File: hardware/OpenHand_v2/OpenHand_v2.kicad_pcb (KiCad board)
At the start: 4 copper layers, 100 x 50 mm, 177 parts, among them J1 CONN_MOTOR_1, J10 CONN_FDBK_2, J2 CONN_MOTOR_2, J3 CONN_BATT, J5 USB_C_CONN, J6 CONN_MOTOR_3, J7 CONN_FDBK_1, Q1 AO3401A, SW1 BTN_RST, SW3 SW_Push, U1 STM32F103RETx, U10 DRV8833PWP, U2 TPS565201DDCR, U3 AMS1117-3.3, U4 LT1175-5_SOT223, U5 LM324, U6 LM324, U7 DRV8833PWP, U8 DRV8833PWP, U9 DRV8833PWP

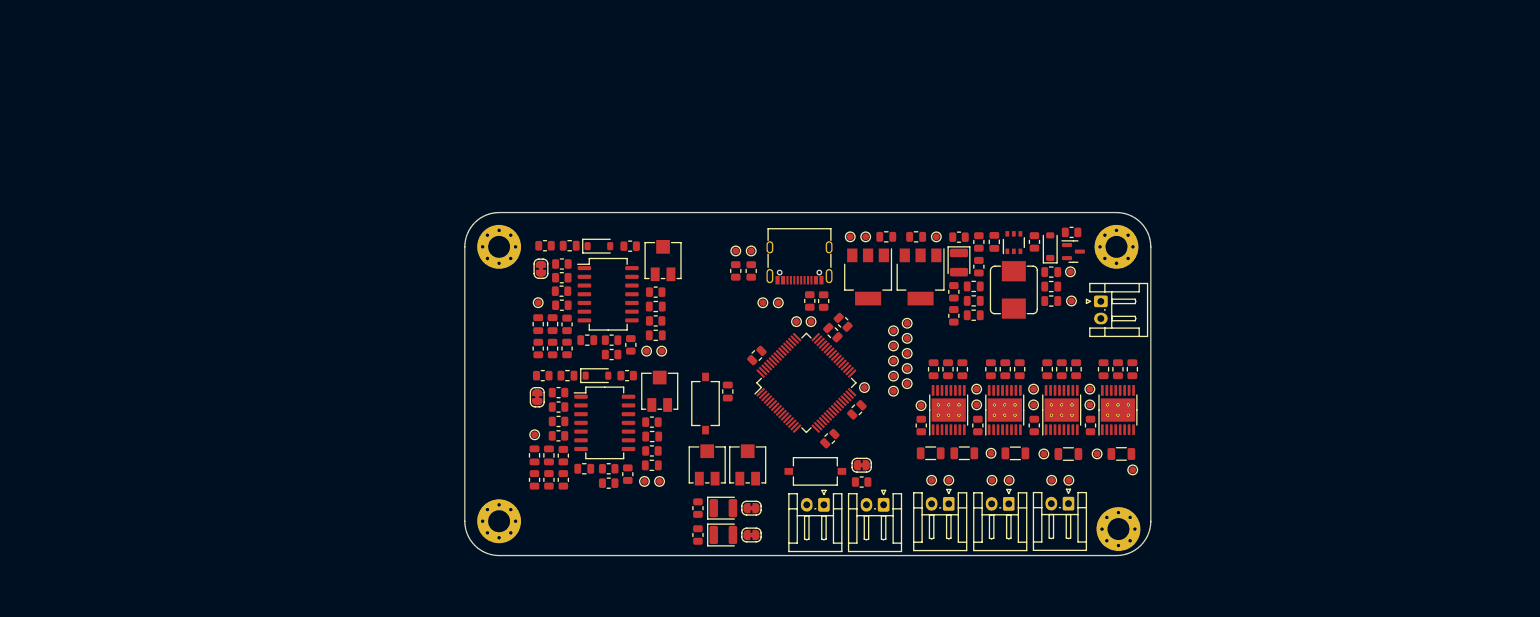
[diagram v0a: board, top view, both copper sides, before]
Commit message: Update V2 schematic and start PCB layout
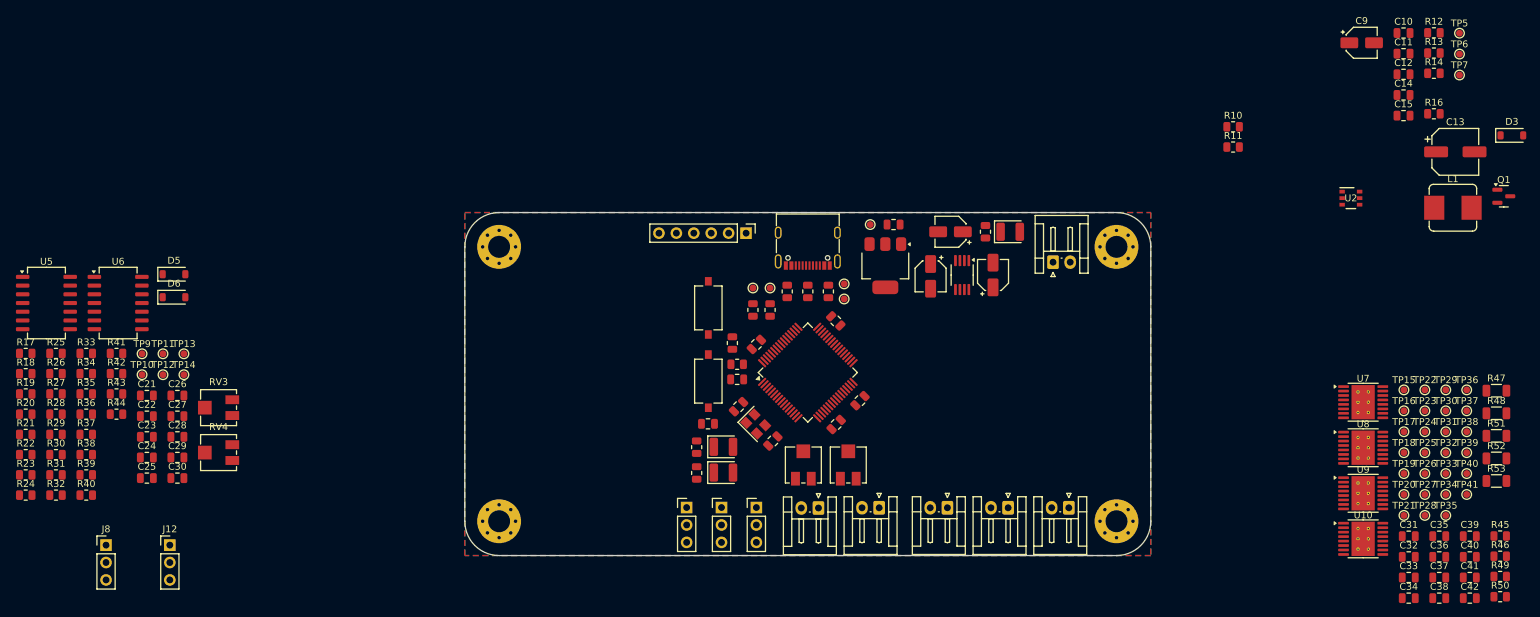
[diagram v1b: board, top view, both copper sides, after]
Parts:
- removed C18: 470n, Capacitor_SMD:C_0805_2012Metric
- removed JP15: JMPR_EMG_1_UC, Jumper:SolderJumper-2_P1.3mm_Bridged_RoundedPad1.0x1.5mm
- removed JP16: JMPR_EMG_2_UC, Jumper:SolderJumper-2_P1.3mm_Bridged_RoundedPad1.0x1.5mm
- removed JP2: JMPR_LED_1, Jumper:SolderJumper-2_P1.3mm_Bridged_RoundedPad1.0x1.5mm
- removed JP3: JMPR_BTN_1, Jumper:SolderJumper-2_P1.3mm_Bridged_RoundedPad1.0x1.5mm
- removed JP4: JMPR_LED_2, Jumper:SolderJumper-2_P1.3mm_Bridged_RoundedPad1.0x1.5mm
- removed R54, R55, R59: 0R2, Resistor_SMD:R_1206_3216Metric
- removed R56, R57: 10k, Resistor_SMD:R_0805_2012Metric
- removed R58, R60: 4R7, Resistor_SMD:R_1206_3216Metric
- removed RV5: 100k, Potentiometer_SMD:Potentiometer_Vishay_TS53YJ_Vertical
- removed SW3: SW_Push, Button_Switch_SMD:SW_Tactile_SPST_NO_Straight_CK_PTS636Sx25SMTRLFS
- removed TP42: TP_MOT_2_UC1, TestPoint:TestPoint_Pad_D1.0mm
- removed TP43: TP_MOT_1_UC2, TestPoint:TestPoint_Pad_D1.0mm
- removed TP44: TP_MOT_2_UC2, TestPoint:TestPoint_Pad_D1.0mm
- removed TP45: TP_MOT_1_OUT_P, TestPoint:TestPoint_Pad_D1.0mm
- removed TP46: TP_MOT_2_OUT_P, TestPoint:TestPoint_Pad_D1.0mm
- removed TP47: TP_MOT_1_OUT_N, TestPoint:TestPoint_Pad_D1.0mm
- removed TP48: TP_MOT_2_OUT_N, TestPoint:TestPoint_Pad_D1.0mm
- removed TP49: TP_MOT_3_EN, TestPoint:TestPoint_Pad_D1.0mm
- removed TP50: TP_FDBK_MOT_EN, TestPoint:TestPoint_Pad_D1.0mm
- removed TP51: TP_MOT_3_IS, TestPoint:TestPoint_Pad_D1.0mm
- removed TP52: TP_MOT_3_FAULT, TestPoint:TestPoint_Pad_D1.0mm
- removed TP53: TP_FDBK_MOT_FAULT, TestPoint:TestPoint_Pad_D1.0mm
- removed TP54: TP_MOT_3_UC1, TestPoint:TestPoint_Pad_D1.0mm
- removed TP55: TP_FDBK_MOT_1_UC1, TestPoint:TestPoint_Pad_D1.0mm
- removed TP56: TP_MOT_3_UC2, TestPoint:TestPoint_Pad_D1.0mm
- removed TP57: TP_FDBK_MOT_1_UC2, TestPoint:TestPoint_Pad_D1.0mm
- removed TP58: TP_MOT_3_OUT_P, TestPoint:TestPoint_Pad_D1.0mm
- removed TP59: TP_MOT_3_OUT_N, TestPoint:TestPoint_Pad_D1.0mm
- removed TP60: TP_FDBK_MOT_2_UC1, TestPoint:TestPoint_Pad_D1.0mm
- removed TP61: TP_FDBK_MOT_2_UC2, TestPoint:TestPoint_Pad_D1.0mm
- added C2: 100n, Capacitor_SMD:C_0805_2012Metric, F.Cu at (142.5, 119.2)
- added C40: 10n, Capacitor_SMD:C_0805_2012Metric, F.Cu at (246.5, 150.2)
- added C41: 10u, Capacitor_SMD:C_0805_2012Metric, F.Cu at (246.5, 153.2)
- added C42: 10u, Capacitor_SMD:C_0805_2012Metric, F.Cu at (246.5, 156.2)
- added J11: CONN_FDBK_2, Connector_JST:JST_EH_S2B-EH_1x02_P2.50mm_Horizontal, F.Cu at (160.4, 143.0)
- added J12: CONN_EMG_2, Connector_PinHeader_2.54mm:PinHeader_1x03_P2.54mm_Vertical, F.Cu at (57.0, 148.5)
- added J13: CONN_POS_3, Connector_PinHeader_2.54mm:PinHeader_1x03_P2.54mm_Vertical, F.Cu at (142.5, 143.0)
- added J4: CONN_POS_1, Connector_PinHeader_2.54mm:PinHeader_1x03_P2.54mm_Vertical, F.Cu at (132.3, 143.0)
- added J8: CONN_EMG_1, Connector_PinHeader_2.54mm:PinHeader_1x03_P2.54mm_Vertical, F.Cu at (47.7, 148.5)
- added J9: CONN_POS_2, Connector_PinHeader_2.54mm:PinHeader_1x03_P2.54mm_Vertical, F.Cu at (137.4, 143.0)
- added R1: 5k1, Resistor_SMD:R_0805_2012Metric, F.Cu at (153.0, 111.5)
- added R13: 54.9k, Resistor_SMD:R_0805_2012Metric, F.Cu at (241.3, 76.8)
- added R14: 47k, Resistor_SMD:R_0805_2012Metric, F.Cu at (241.3, 79.7)
- added R15: 4k7, Resistor_SMD:R_0805_2012Metric, F.Cu at (175.9, 102.8)
- added R16: 10k, Resistor_SMD:R_0805_2012Metric, F.Cu at (241.3, 85.6)
- added R5: 4k7, Resistor_SMD:R_0805_2012Metric, F.Cu at (144.5, 114.2)
- added RV3: 100k, Potentiometer_SMD:Potentiometer_Vishay_TS53YJ_Vertical, F.Cu at (64.1, 128.4)
- added SW2: SW_Push, Button_Switch_SMD:SW_Tactile_SPST_NO_Straight_CK_PTS636Sx25SMTRLFS, F.Cu at (135.5, 113.9)
- added TP1: TP_UC_TX, TestPoint:TestPoint_Pad_D1.0mm, F.Cu at (155.3, 110.4)
- added TP10: TP_EMG_2_AMP, TestPoint:TestPoint_Pad_D1.0mm, F.Cu at (53.0, 123.6)
- added TP11: TP_EMG_1_HP, TestPoint:TestPoint_Pad_D1.0mm, F.Cu at (56.0, 120.6)
- added TP12: TP_EMG_2_HP, TestPoint:TestPoint_Pad_D1.0mm, F.Cu at (56.0, 123.6)
- added TP13: TP_EMG_1_LP, TestPoint:TestPoint_Pad_D1.0mm, F.Cu at (59.1, 120.6)
- added TP14: TP_EMG_2_LP, TestPoint:TestPoint_Pad_D1.0mm, F.Cu at (59.1, 123.6)
- added TP15: TP_MOT_1_EN, TestPoint:TestPoint_Pad_D1.0mm, F.Cu at (236.9, 125.8)
- added TP16: TP_MOT_2_EN, TestPoint:TestPoint_Pad_D1.0mm, F.Cu at (236.9, 128.9)
- added TP17: TP_MOT_1_IS, TestPoint:TestPoint_Pad_D1.0mm, F.Cu at (236.9, 131.9)
- added TP20: TP_MOT_2_FAULT, TestPoint:TestPoint_Pad_D1.0mm, F.Cu at (236.9, 141.1)
- added TP4: TP_UC_SDA, TestPoint:TestPoint_Pad_D1.0mm, F.Cu at (142.0, 111.0)
- added TP5: TP_BATT_P, TestPoint:TestPoint_Pad_D1.0mm, F.Cu at (245.0, 73.8)
- added TP6: TP_V_BATT, TestPoint:TestPoint_Pad_D1.0mm, F.Cu at (245.0, 76.9)
- added TP7: TP_V_5V, TestPoint:TestPoint_Pad_D1.0mm, F.Cu at (245.0, 80.0)
- added TP8: TP_V_3V3, TestPoint:TestPoint_Pad_D1.0mm, F.Cu at (159.1, 101.8)
- added TP9: TP_EMG_1_AMP, TestPoint:TestPoint_Pad_D1.0mm, F.Cu at (53.0, 120.6)
- added Y1: 16MHz, Crystal:Crystal_SMD_3225-4Pin_3.2x2.5mm, F.Cu at (142.4, 130.8)
- C10: value 100n -> 10u
- C11, C15: value 22u -> 1u
- C12: value 22u -> 100n
- C13: value 1u -> 47u; footprint Capacitor_SMD:C_0805_2012Metric -> Capacitor_SMD:CP_Elec_6.3x5.4
- C16: value 100n -> 10u; footprint Capacitor_SMD:C_0805_2012Metric -> Capacitor_SMD:CP_Elec_4x5.4
- C17: value 100n -> 22u
- C19, C20: value 470n -> 10u; footprint Capacitor_SMD:C_0805_2012Metric -> Capacitor_SMD:CP_Elec_4x5.4
- C21, C22: value 470n -> 100n
- C24, C25: value 330n -> 470n
- C26, C27: value 10u -> 470n
- C28: value 2u2 -> 470n
- C29: value 2u2 -> 330n
- C30: value 10n -> 330n
- C31, C37: value 10n -> 2u2
- C32, C38: value 10u -> 2u2
- C33, C39: value 10u -> 10n
- C34: value 2u2 -> 10n
- C35: value 2u2 -> 10u
- C36: value 10n -> 10u
- C6: value 100n -> 1u
- C7, C8: value 10u -> 10p
- C9: value 1u -> 10u; footprint Capacitor_SMD:C_0805_2012Metric -> Capacitor_SMD:CP_Elec_4x5.4
- J10: value CONN_FDBK_2 -> CONN_JTAG; footprint Connector_JST:JST_EH_S2B-EH_1x02_P2.50mm_Horizontal -> Connector_PinHeader_2.54mm:PinHeader_1x06_P2.54mm_Vertical
- J5: value USB_C_CONN -> CONN_USB_C
- R10: value 4k7 -> 47k
- R11, R32, R42: value 47k -> 10k
- R17, R37: value 10k -> 47k
- R18: value 54.9k -> 15k
- R20: value 4k7 -> 15k
- R21: value 10k -> 1k
- R22, R24, R35: value 47k -> 1k
- R23, R25, R36: value 15k -> 1k
- R27, R30: value 1k -> 47k
- R28, R31: value 1k -> 15k
- R29, R41, R45: value 1k -> 10k
- R3: value 5k1 -> 1.5k
- R33: value 15k -> 18k
- R34: value 10k -> 18k
- R38: value 18k -> 47k
- R39: value 18k -> 1k
- R4: value 1.5k -> 4k7
- R43: value 47k -> 18k
- R44: value 1k -> 18k
- R47, R52: value 10k -> 0R2; footprint Resistor_SMD:R_0805_2012Metric -> Resistor_SMD:R_1206_3216Metric
- R48: value 18k -> 0R2; footprint Resistor_SMD:R_0805_2012Metric -> Resistor_SMD:R_1206_3216Metric
- R49, R50: value 18k -> 10k
- R51: value 18k -> 4R7; footprint Resistor_SMD:R_0805_2012Metric -> Resistor_SMD:R_1206_3216Metric
- R53: value 10k -> 4R7; footprint Resistor_SMD:R_0805_2012Metric -> Resistor_SMD:R_1206_3216Metric
- R6, R9: value 4k7 -> 10k
- R8: value 10k -> 4k7
- TP18: value TP_UC_TX -> TP_MOT_1_FAULT
- TP19: value TP_UC_RX -> TP_MOT_2_IS
- TP2: value TP_USB_D_P -> TP_UC_RX
- TP21: value TP_UC_SCL -> TP_MOT_1_UC1
- TP22: value TP_UC_SDA -> TP_MOT_2_UC1
- TP23: value TP_UC_PIN_PB12 -> TP_MOT_1_UC2
- TP24: value TP_BATT_P -> TP_MOT_2_UC2
- TP25: value TP_V_BATT -> TP_MOT_1_OUT_P
- TP26: value TP_V_5V -> TP_MOT_2_OUT_P
- TP27: value TP_V_3V3 -> TP_MOT_1_OUT_N
- TP28: value TP_V_N5V -> TP_MOT_2_OUT_N
- TP29: value TP_EMG_1_AMP -> TP_MOT_3_EN
- TP3: value TP_USB_D_N -> TP_UC_SCL
- TP30: value TP_EMG_2_AMP -> TP_FDBK_MOT_EN
- TP31: value TP_EMG_1_HP -> TP_MOT_3_IS
- TP32: value TP_EMG_2_HP -> TP_MOT_3_FAULT
- TP33: value TP_EMG_1_LP -> TP_FDBK_MOT_FAULT
- TP34: value TP_EMG_2_LP -> TP_MOT_3_UC1
- TP35: value TP_MOT_1_EN -> TP_FDBK_MOT_1_UC1
- TP36: value TP_MOT_2_EN -> TP_MOT_3_UC2
- TP37: value TP_MOT_1_IS -> TP_FDBK_MOT_1_UC2
- TP38: value TP_MOT_1_FAULT -> TP_MOT_3_OUT_P
- TP39: value TP_MOT_2_IS -> TP_MOT_3_OUT_N
- TP40: value TP_MOT_2_FAULT -> TP_FDBK_MOT_2_UC1
- TP41: value TP_MOT_1_UC1 -> TP_FDBK_MOT_2_UC2
- U4: value LT1175-5_SOT223 -> ICL7660; footprint Package_TO_SOT_SMD:SOT-223-3_TabPin2 -> Package_SO:MSOP-8_3x3mm_P0.65mm
- moved R19 154.3 mm to (36.0, 126.4), turned to 0 degrees
- moved R17 147.9 mm to (36.0, 120.5), turned to 0 degrees
- moved R21 141.7 mm to (36.0, 132.3), turned to 0 degrees
- moved R48 140.8 mm to (250.4, 129.3), turned to 0 degrees
- moved R18 139.8 mm to (36.0, 123.5), turned to 0 degrees
- moved R51 139.3 mm to (250.4, 132.6), turned to 0 degrees
- moved R20 138.5 mm to (36.0, 129.4)
- moved TP29 132.9 mm to (243.0, 125.8), turned to 0 degrees
- moved TP30 132.9 mm to (243.0, 128.9), turned to 0 degrees
- moved R46 130.4 mm to (250.9, 150.1), turned to 0 degrees
- moved R49 128.6 mm to (250.9, 153.1)
- moved C29 127.5 mm to (58.1, 135.7), turned to 0 degrees
- moved R47 127.2 mm to (250.4, 126.0), turned to 0 degrees
- moved R50 125.5 mm to (250.9, 156.0)
- moved R45 124.8 mm to (250.9, 147.2)
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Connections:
- C1 pad 2: Earth -> GND
- C10 pad 1: Net-(U2-SW) -> +BATT
- C10 pad 2: Net-(U2-VBST) -> GND
- C11 pad 1: +5V -> +BATT
- C11 pad 2: Earth -> GND
- C12 pad 1: +5V -> Net-(U2-SW)
- C12 pad 2: Earth -> Net-(U2-VBST)
- C13 pad 2: Earth -> GND
- C14 pad 1: +3V3 -> +5V
- C14 pad 2: Earth -> GND
- C15 pad 1: -5V -> +5V
- C15 pad 2: Earth -> GND
- C16 pad 1: +5V -> GND
- C16 pad 2: Earth -> -5V
- C17 pad 1: +5V -> +3V3
- C17 pad 2: Earth -> GND
- C19 pad 1: Net-(C18-Pad2) -> +5V
- C19 pad 2: Net-(U5B-+) -> GND
- C20 pad 1: Net-(C20-Pad1) -> Net-(U4-CAP+)
- C20 pad 2: Net-(C20-Pad2) -> Net-(U4-CAP-)
- C21 pad 1: Net-(C20-Pad2) -> +5V
- C21 pad 2: Net-(U6B-+) -> GND
- C22 pad 1: EMG_1_MIDPOINT -> +5V
- C22 pad 2: Net-(U5D-+) -> GND
- C23 pad 1: EMG_2_MIDPOINT -> Net-(C23-Pad1)
- C23 pad 2: Net-(U6D-+) -> Net-(C23-Pad2)
- C24 pad 1: Earth -> Net-(C23-Pad2)
- C24 pad 2: Net-(U5C-+) -> Net-(U5B-+)
- C25 pad 1: Earth -> Net-(C25-Pad1)
- C25 pad 2: Net-(U6C-+) -> Net-(C25-Pad2)
- C26 pad 1: Net-(D5-K) -> Net-(C25-Pad2)
- C26 pad 2: Earth -> Net-(U6B-+)
- C27 pad 1: Net-(D6-K) -> EMG_1_MIDPOINT
- C27 pad 2: Earth -> Net-(U5D-+)
- C28 pad 1: Earth -> EMG_2_MIDPOINT
- C28 pad 2: Net-(U7-VINT) -> Net-(U6D-+)
- C29 pad 1: Earth -> GND
- C29 pad 2: Net-(U8-VINT) -> Net-(U5C-+)
- C3 pad 2: Earth -> GND
- C30 pad 1: +5V -> GND
- C30 pad 2: Net-(U7-VCP) -> Net-(U6C-+)
- C31 pad 1: +5V -> GND
- C31 pad 2: Net-(U8-VCP) -> Net-(U7-VINT)
- C32 pad 1: +5V -> GND
- C32 pad 2: Earth -> Net-(U8-VINT)
- C33 pad 2: Earth -> Net-(U7-VCP)
- C34 pad 1: Earth -> +5V
- C34 pad 2: Net-(U9-VINT) -> Net-(U8-VCP)
- C35 pad 1: Earth -> +5V
- C35 pad 2: Net-(U10-VINT) -> GND
- C36 pad 2: Net-(U9-VCP) -> GND
- C37 pad 1: +5V -> GND
- C37 pad 2: Net-(U10-VCP) -> Net-(U9-VINT)
- C38 pad 1: +5V -> GND
- C38 pad 2: Earth -> Net-(U10-VINT)
- C39 pad 2: Earth -> Net-(U9-VCP)
- C4 pad 2: Earth -> GND
- C5 pad 2: Earth -> GND
- C6 pad 2: Earth -> GND
- C7 pad 1: +BATT -> /HSE_IN
- C7 pad 2: Earth -> GND
- C8 pad 1: +BATT -> /HSE_OUT
- C8 pad 2: Earth -> GND
- C9 pad 2: Earth -> GND
- D1 pad 1: Net-(D1-K) -> /LED_1_K
- D1 pad 2: Net-(D1-A) -> LED_1
- D2 pad 1: Net-(D2-K) -> /LED_2_K
- D2 pad 2: Net-(D2-A) -> LED_2
- D5 pad 1: Net-(D5-K) -> EMG_01_UC
- D6 pad 1: Net-(D6-K) -> EMG_02_UC
- H1 pad 1: Earth -> GND
- H2 pad 1: Earth -> GND
- H3 pad 1: Earth -> GND
- H4 pad 1: Earth -> GND
- J10 pad 1: HAPTIC_02_N -> GND
- J10 pad 2: HAPTIC_02_P -> JTAG_RST
- J3 pad 1: Earth -> GND
- J5 pad A1: Earth -> GND
- J5 pad A12: Earth -> GND
- J5 pad A5: Net-(J5-CC1) -> /USB_CC1
- J5 pad B1: Earth -> GND
- J5 pad B12: Earth -> GND
- J5 pad B5: Net-(J5-CC2) -> /USB_CC2
- R10 pad 1: Net-(D2-K) -> /BATT_SENSE
- R10 pad 2: Earth -> +BATT
- R11 pad 1: /BATT_SENSE -> GND
- R11 pad 2: +BATT -> /BATT_SENSE
- R12 pad 1: Earth -> Net-(U2-EN)
- R12 pad 2: /BATT_SENSE -> +BATT
- R17 pad 1: Net-(U2-EN) -> GND
- R17 pad 2: +BATT -> Net-(U5A-+)
- R18 pad 1: +5V -> Net-(C23-Pad2)
- R18 pad 2: Net-(U2-VFB) -> Net-(R18-Pad2)
- R19 pad 1: Earth -> GND
- R19 pad 2: Net-(D3-A) -> Net-(U6A-+)
- R2 pad 1: Net-(J5-CC1) -> /USB_CC2
- R2 pad 2: Earth -> GND
- R20 pad 1: Net-(D4-K) -> Net-(C25-Pad2)
- R20 pad 2: Earth -> Net-(R20-Pad2)
- R21 pad 1: Net-(U2-VFB) -> Net-(U5A-+)
- R21 pad 2: Earth -> EMG_01_P
- R22 pad 1: Earth -> Net-(U6A-+)
- R22 pad 2: Net-(U5A-+) -> EMG_02_P
- R23 pad 1: Net-(C18-Pad2) -> Net-(U5A--)
- R23 pad 2: Net-(R23-Pad2) -> EMG_01_N
- R24 pad 1: Earth -> Net-(R18-Pad2)
- R24 pad 2: Net-(U6A-+) -> EMG_1_MIDPOINT
- R25 pad 1: Net-(C20-Pad2) -> Net-(U6A--)
- R25 pad 2: Net-(R25-Pad2) -> EMG_02_N
- R26 pad 1: Net-(U5A-+) -> Net-(R20-Pad2)
- R26 pad 2: EMG_01_P -> EMG_2_MIDPOINT
- R27 pad 1: Net-(U6A-+) -> Net-(U5A--)
- R27 pad 2: EMG_02_P -> Net-(C23-Pad1)
- R28 pad 1: Net-(U5A--) -> Net-(U5B-+)
- R28 pad 2: EMG_01_N -> GND
- R29 pad 1: Net-(R23-Pad2) -> Net-(U5B--)
- R29 pad 2: EMG_1_MIDPOINT -> Net-(R18-Pad2)
- R3 pad 1: Net-(J5-CC2) -> USB_D+
- R3 pad 2: Earth -> +3V3
- R30 pad 2: EMG_02_N -> Net-(C25-Pad1)
- R31 pad 1: Net-(R25-Pad2) -> Net-(U6B-+)
- R31 pad 2: EMG_2_MIDPOINT -> GND
- R32 pad 1: Net-(U5A--) -> Net-(U6B--)
- R32 pad 2: /Sensors/amp_out_1 -> Net-(R20-Pad2)
- R33 pad 1: Net-(U5B-+) -> Net-(U5B--)
- R33 pad 2: Earth -> GND
- R34 pad 1: Net-(U5B--) -> Net-(U6B--)
- R34 pad 2: Net-(R23-Pad2) -> GND
- R35 pad 1: Net-(U6A--) -> EMG_1_MIDPOINT
- R35 pad 2: Net-(C20-Pad1) -> Net-(U5C-+)
- R36 pad 1: Net-(U6B-+) -> EMG_2_MIDPOINT
- R36 pad 2: Earth -> Net-(U6C-+)
- R37 pad 1: Net-(U6B--) -> Net-(D6-A)
- R37 pad 2: Net-(R25-Pad2) -> Net-(R37-Pad2)
- R38 pad 1: Net-(U5B--) -> Net-(D5-A)
- R38 pad 2: Earth -> Net-(R38-Pad2)
- R39 pad 1: Net-(U6B--) -> Net-(U5D--)
- R39 pad 2: Earth -> GND
- R4 pad 1: USB_D- -> UC_SDA
- R40 pad 1: EMG_1_MIDPOINT -> Net-(U6D--)
- R40 pad 2: Net-(U5C-+) -> GND
- R41 pad 1: EMG_2_MIDPOINT -> Net-(U5C--)
- R41 pad 2: Net-(U6C-+) -> Net-(U5D-+)
- R42 pad 1: Net-(D6-A) -> Net-(U6C--)
- R42 pad 2: Net-(R42-Pad2) -> Net-(U6D-+)
- R43 pad 1: Net-(D5-A) -> Net-(U5C--)
- R43 pad 2: Net-(R43-Pad2) -> GND
- R44 pad 1: Net-(U5D--) -> Net-(U6C--)
- R44 pad 2: Earth -> GND
- R45 pad 1: Net-(U6D--) -> MOTOR_01_EN
- R45 pad 2: Earth -> +5V
- R46 pad 1: Net-(U5C--) -> MOTOR_02_EN
- R46 pad 2: Net-(U5D-+) -> +5V
- R47 pad 1: Net-(U6C--) -> GND
- R47 pad 2: Net-(U6D-+) -> Net-(U7-AISEN)
- R48 pad 1: Net-(D5-K) -> GND
- R48 pad 2: Earth -> Net-(U8-AISEN)
- R49 pad 1: Net-(U5C--) -> MOTOR_03_EN
- R49 pad 2: Earth -> +5V
- R50 pad 1: Net-(U6C--) -> HAPTIC_EN
- R50 pad 2: Earth -> +5V
- R51 pad 1: Net-(D6-K) -> GND
- R51 pad 2: Earth -> Net-(U10-AISEN)
- R52 pad 1: MOTOR_01_EN -> GND
- R52 pad 2: +5V -> Net-(U9-AISEN)
- R53 pad 1: MOTOR_02_EN -> GND
- R53 pad 2: +5V -> Net-(U10-BISEN)
- R6 pad 1: UC_SDA -> +3V3
- R6 pad 2: +3V3 -> BTN_01
- R7 pad 1: UC_SCL -> /LED_1_K
- R7 pad 2: +3V3 -> GND
- R8 pad 1: +3V3 -> /LED_2_K
- R8 pad 2: Net-(JP3-A) -> GND
- R9 pad 1: Net-(D1-K) -> GND
- R9 pad 2: Earth -> /UC_BOOT
- RV1 pad 1: Earth -> GND
- RV1 pad 2: Net-(JP1-A) -> TRIM_POT_01
- RV2 pad 1: Earth -> GND
- RV2 pad 2: Net-(JP5-A) -> TRIM_POT_02
- RV4 pad 1: Net-(R43-Pad2) -> Net-(R37-Pad2)
- RV4 pad 2: Net-(R43-Pad2) -> Net-(R37-Pad2)
- RV4 pad 3: Net-(U5D--) -> Net-(U6D--)
- SW1 pad 2: Earth -> GND
- TP18 pad 1: UC_TX -> MOTOR_01_FAULT
- TP19 pad 1: UC_RX -> Net-(U8-AISEN)
- TP2 pad 1: USB_D+ -> UC_RX
- TP21 pad 1: UC_SCL -> MOTOR_01_DIR
- TP22 pad 1: UC_SDA -> MOTOR_02_DIR
- TP23 pad 1: Net-(U1-PB12) -> MOTOR_01_PWM
- TP24 pad 1: BAT_P -> MOTOR_02_PWM
- TP25 pad 1: +BATT -> MOTOR_01_P
- TP26 pad 1: +5V -> MOTOR_02_P
- TP27 pad 1: +3V3 -> MOTOR_01_N
- TP28 pad 1: -5V -> MOTOR_02_N
- TP29 pad 1: /Sensors/amp_out_1 -> MOTOR_03_EN
- TP3 pad 1: USB_D- -> UC_SCL
- TP30 pad 1: Net-(C20-Pad1) -> HAPTIC_EN
- TP31 pad 1: EMG_1_MIDPOINT -> Net-(U9-AISEN)
- TP32 pad 1: EMG_2_MIDPOINT -> MOTOR_03_FAULT
- TP33 pad 1: Net-(U5D-+) -> HAPTIC_FAULT
- TP34 pad 1: Net-(U6D-+) -> MOTOR_03_DIR
- TP35 pad 1: MOTOR_01_EN -> HAPTIC_01_DIR
- TP36 pad 1: MOTOR_02_EN -> MOTOR_03_PWM
- TP37 pad 1: Net-(U7-AISEN) -> HAPTIC_01_PWM
- TP38 pad 1: MOTOR_01_FAULT -> MOTOR_03_P
- TP39 pad 1: Net-(U8-AISEN) -> MOTOR_03_N
- TP40 pad 1: MOTOR_02_FAULT -> HAPTIC_02_DIR
- TP41 pad 1: MOTOR_01_DIR -> HAPTIC_02_PWM
- U1 pad 12: Earth -> GND
- U1 pad 14: TRIM_POT_03 -> unconnected-(U1-PA0-Pad14)
- U1 pad 18: Earth -> GND
- U1 pad 2: HW_REV_01 -> unconnected-(U1-PC13-Pad2)
- U1 pad 21: Net-(U1-PA5) -> unconnected-(U1-PA5-Pad21)
- U1 pad 22: Net-(U1-PA6) -> unconnected-(U1-PA6-Pad22)
- U1 pad 3: HW_REV_02 -> unconnected-(U1-PC14-Pad3)
- U1 pad 31: Earth -> GND
- U1 pad 33: Net-(U1-PB12) -> unconnected-(U1-PB12-Pad33)
- U1 pad 4: HW_REV_03 -> unconnected-(U1-PC15-Pad4)
- U1 pad 47: Earth -> GND
- U1 pad 5: HW_REV_04 -> /HSE_IN
- U1 pad 53: Net-(U1-PC12) -> unconnected-(U1-PC12-Pad53)
- U1 pad 54: Net-(U1-PD2) -> unconnected-(U1-PD2-Pad54)
- U1 pad 6: unconnected-(U1-PD1-Pad6) -> /HSE_OUT
- U1 pad 60: Net-(U1-BOOT0) -> /UC_BOOT
- U1 pad 63: Earth -> GND
- U10 pad 13: Earth -> GND
- U10 pad 17: Earth -> GND
- U2 pad 1: Earth -> GND
- U3 pad 1: Earth -> GND
- U4 pad 1: -5V -> unconnected-(U4-NC-Pad1)
- U4 pad 2: +BATT -> Net-(U4-CAP+)
- U4 pad 3: Earth -> GND
- U5 pad 1: /Sensors/amp_out_1 -> Net-(C23-Pad1)
- U5 pad 7: Net-(R23-Pad2) -> Net-(R18-Pad2)
- U6 pad 1: Net-(C20-Pad1) -> Net-(C25-Pad1)
- U6 pad 7: Net-(R25-Pad2) -> Net-(R20-Pad2)
- U7 pad 13: Earth -> GND
- U7 pad 17: Earth -> GND
- U8 pad 13: Earth -> GND
- U8 pad 17: Earth -> GND
- U9 pad 13: Earth -> GND
- U9 pad 17: Earth -> GND
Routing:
- added copper zone on In1.Cu, net +3V3
- added copper zone on In1.Cu, net +5V
- added copper zone on B.Cu, net GND
- added copper zone on F.Cu, net GND
- added copper zone on In2.Cu, net GND

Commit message: Add V2 PCB and update CubeIDE config for V2
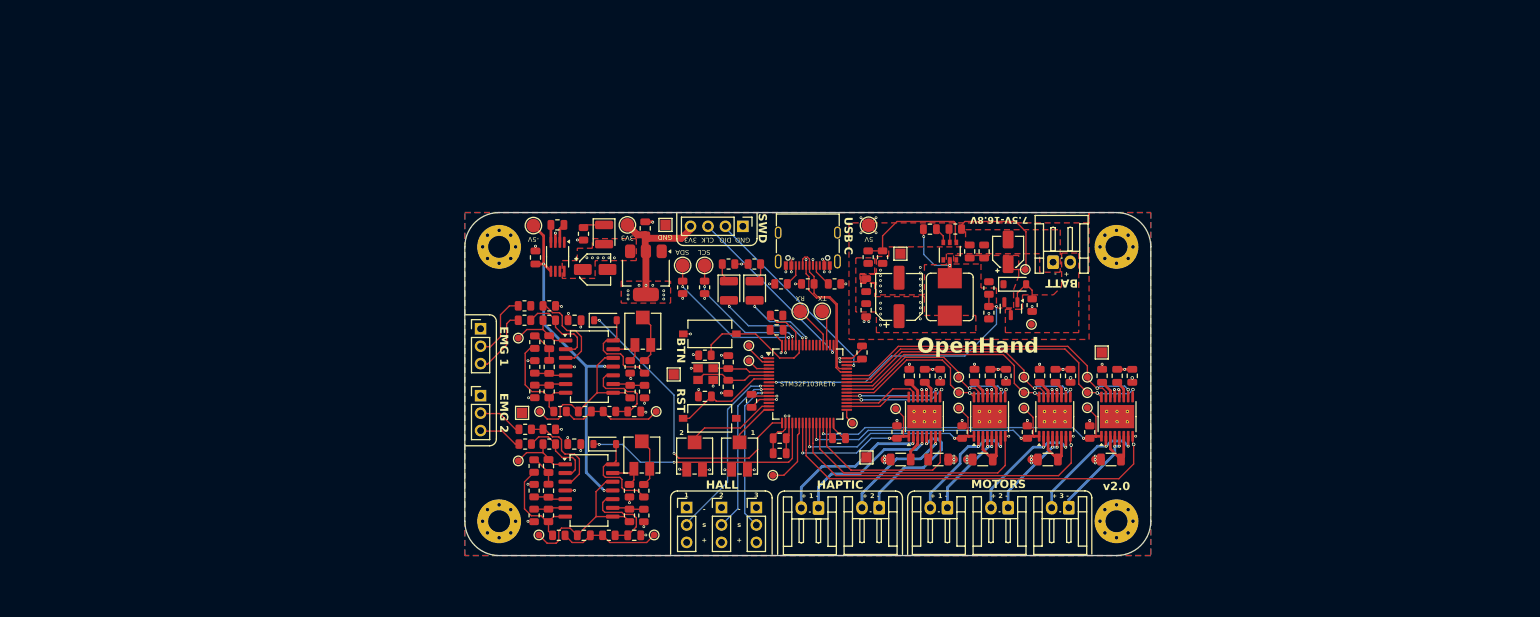
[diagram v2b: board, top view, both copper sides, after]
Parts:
- removed the C16 at (167.9, 109.3)
- removed the J10 at (141.0, 103.0)
- removed the TP17 at (236.9, 131.9)
- removed the TP19 at (236.9, 138.1)
- removed the TP20 at (236.9, 141.1)
- removed the TP25 at (239.9, 135.0)
- removed the TP26 at (239.9, 138.1)
- removed the TP27 at (239.9, 141.1)
- removed the TP28 at (239.9, 144.2)
- removed the TP30 at (243.0, 128.9)
- removed the TP31 at (243.0, 131.9)
- removed the TP32 at (243.0, 135.0)
- removed the TP35 at (243.0, 144.2)
- removed TP37: TP_FDBK_MOT_1_UC2, TestPoint:TestPoint_Pad_D1.0mm
- removed TP38: TP_MOT_3_OUT_P, TestPoint:TestPoint_Pad_D1.0mm
- removed TP39: TP_MOT_3_OUT_N, TestPoint:TestPoint_Pad_D1.0mm
- removed TP40: TP_FDBK_MOT_2_UC1, TestPoint:TestPoint_Pad_D1.0mm
- removed TP41: TP_FDBK_MOT_2_UC2, TestPoint:TestPoint_Pad_D1.0mm
- added C17: 10u, Capacitor_SMD:C_0805_2012Metric, F.Cu at (110.3, 106.5)
- added C6: 100n, Capacitor_SMD:C_0805_2012Metric, F.Cu at (141.8, 127.5)
- added J12: CONN_SWD, Connector_PinHeader_2.54mm:PinHeader_1x04_P2.54mm_Vertical, F.Cu at (140.5, 102.0)
- added TP1: TP_UC_PA6, TestPoint:TestPoint_Pad_D1.0mm, F.Cu at (144.9, 138.3)
- added TP10: TP_GND_5, TestPoint:TestPoint_Pad_1.5x1.5mm, F.Cu at (158.6, 135.7)
- added TP11: TP_GND_6, TestPoint:TestPoint_Pad_1.5x1.5mm, F.Cu at (163.5, 106.0)
- added TP14: TP_UC_PB12, TestPoint:TestPoint_Pad_D1.0mm, F.Cu at (156.5, 130.7)
- added TP4: TP_UC_PC13, TestPoint:TestPoint_Pad_D1.0mm, F.Cu at (141.4, 119.4)
- added TP5: TP_UC_PC15, TestPoint:TestPoint_Pad_D1.0mm, F.Cu at (141.4, 121.6)
- added TP6: TP_GND_1, TestPoint:TestPoint_Pad_1.5x1.5mm, F.Cu at (108.3, 129.2)
- added TP7: TP_GND_2, TestPoint:TestPoint_Pad_1.5x1.5mm, F.Cu at (129.2, 101.8)
- added TP8: TP_GND_3, TestPoint:TestPoint_Pad_1.5x1.5mm, F.Cu at (192.8, 120.4)
- added TP9: TP_GND_4, TestPoint:TestPoint_Pad_1.5x1.5mm, F.Cu at (130.4, 123.6)
- C18: renamed from C17; value 22u -> 10u
- C20: footprint Capacitor_SMD:CP_Elec_4x5.4 -> Capacitor_SMD:C_0805_2012Metric
- TP12: renamed from TP3; footprint TestPoint:TestPoint_Pad_D1.0mm -> TestPoint:TestPoint_Pad_D2.0mm
- TP13: renamed from TP4; footprint TestPoint:TestPoint_Pad_D1.0mm -> TestPoint:TestPoint_Pad_D2.0mm
- TP17: renamed from TP7; footprint TestPoint:TestPoint_Pad_D1.0mm -> TestPoint:TestPoint_Pad_D2.0mm
- TP18: value TP_MOT_1_FAULT -> TP_V_N5V; footprint TestPoint:TestPoint_Pad_D1.0mm -> TestPoint:TestPoint_Pad_D2.0mm
- TP19: renamed from TP8; footprint TestPoint:TestPoint_Pad_D1.0mm -> TestPoint:TestPoint_Pad_D2.0mm
- TP2: renamed from TP1; footprint TestPoint:TestPoint_Pad_D1.0mm -> TestPoint:TestPoint_Pad_D2.0mm
- TP3: renamed from TP2; footprint TestPoint:TestPoint_Pad_D1.0mm -> TestPoint:TestPoint_Pad_D2.0mm
- TP33: value TP_FDBK_MOT_FAULT -> TP_FDBK_MOT_EN
- moved TP18 131.1 mm to (110.0, 101.9)
- moved R50 91.1 mm to (163.0, 132.0), turned to 90 degrees
- moved TP17 88.9 mm to (158.8, 101.8)
- moved R13 87.7 mm to (158.8, 106.5), turned to 90 degrees
- moved R51 86.9 mm to (163.5, 136.0)
- moved C15 84.4 mm to (158.5, 114.2), turned to -90 degrees
- moved C14 83.8 mm to (163.3, 112.3), turned to 90 degrees
- moved C38 83.8 mm to (164.8, 123.8), turned to -90 degrees
- moved C42 83.7 mm to (169.3, 123.8), turned to -90 degrees
- moved C40 83.7 mm to (167.1, 123.8), turned to -90 degrees
- moved R16 83.0 mm to (160.9, 106.5), turned to -90 degrees
- moved R38 82.4 mm to (126.2, 122.5), turned to 90 degrees
- moved C16 82.1 mm to (158.5, 110.6), turned to 90 degrees
- moved R37 81.7 mm to (126.1, 140.6), turned to 90 degrees
- moved R53 81.4 mm to (169.0, 136.0), turned to 180 degrees
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- renumbered C9 to C10, C10 to C11, C11 to C12, C12 to C13, C13 to C14, C14 to C15, C15 to C16, C6 to C7, C7 to C8, C8 to C9, J11 to J10, J12 to J11, TP5 to TP15, TP6 to TP16, TP9 to TP20, TP10 to TP21, TP11 to TP22, TP12 to TP23, TP13 to TP24, TP14 to TP25, TP15 to TP26, TP16 to TP27, TP21 to TP28, TP22 to TP29, TP23 to TP30, TP24 to TP31, TP29 to TP32, TP36 to TP35
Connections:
- net Net-(D3-A) renamed /PSU/REVP_MOS_GATE
- net Net-(D4-K) renamed /PSU/PSU_LED_K
- net Net-(U2-EN) renamed /PSU/PSU_EN
- net Net-(U2-SW) renamed /PSU/PSU_SW
- net Net-(U2-VBST) renamed /PSU/PSU_VBST
- net Net-(U2-VFB) renamed /PSU/PSU_VFB
- TP18 pad 1: MOTOR_01_FAULT -> -5V
- TP33 pad 1: HAPTIC_FAULT -> HAPTIC_EN
- U1 pad 2: unconnected-(U1-PC13-Pad2) -> Net-(U1-PC13)
- U1 pad 22: unconnected-(U1-PA6-Pad22) -> Net-(U1-PA6)
- U1 pad 23: MOTOR_01_EN -> HAPTIC_EN
- U1 pad 24: MOTOR_02_EN -> MOTOR_03_FAULT
- U1 pad 25: MOTOR_03_EN -> MOTOR_01_EN
- U1 pad 26: HAPTIC_EN -> MOTOR_02_FAULT
- U1 pad 27: MOTOR_01_FAULT -> MOTOR_02_EN
- U1 pad 28: MOTOR_02_FAULT -> MOTOR_01_FAULT
- U1 pad 29: MOTOR_03_FAULT -> MOTOR_03_EN
- U1 pad 33: unconnected-(U1-PB12-Pad33) -> Net-(U1-PB12)
- U1 pad 34: HAPTIC_02_DIR -> HAPTIC_01_DIR
- U1 pad 35: HAPTIC_02_PWM -> HAPTIC_01_PWM
- U1 pad 36: HAPTIC_01_DIR -> HAPTIC_02_DIR
- U1 pad 37: HAPTIC_01_PWM -> HAPTIC_02_PWM
- U1 pad 38: MOTOR_03_DIR -> MOTOR_01_DIR
- U1 pad 39: MOTOR_03_PWM -> MOTOR_01_PWM
- U1 pad 4: unconnected-(U1-PC15-Pad4) -> Net-(U1-PC15)
- U1 pad 42: MOTOR_01_DIR -> MOTOR_03_DIR
- U1 pad 43: MOTOR_01_PWM -> MOTOR_03_PWM
- U1 pad 46: JTAG_TMS -> SWDIO
- U1 pad 49: JTAG_TCK -> SWCLK
- U1 pad 50: JTAG_TDI -> unconnected-(U1-PA15-Pad50)
- U1 pad 55: JTAG_TDO -> unconnected-(U1-PB3-Pad55)
- U1 pad 56: JTAG_RST -> unconnected-(U1-PB4-Pad56)
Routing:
- net GND: track 0.00 -> 67.0 mm, vias 0 -> 76
- net MOTOR_03_FAULT: track 0.00 -> 59.4 mm, vias 0 -> 2
- net -5V: track 0.00 -> 50.5 mm, vias 0 -> 3
- net MOTOR_03_DIR: track 0.00 -> 50.2 mm, vias 0 -> 2
- net MOTOR_03_PWM: track 0.00 -> 50.1 mm, vias 0 -> 2
- net MOTOR_02_FAULT: track 0.00 -> 48.5 mm, vias 0 -> 2
- net MOTOR_03_EN: track 0.00 -> 48.0 mm, vias 0 -> 2
- net +3V3: track 0.00 -> 47.0 mm, vias 0 -> 20
- net EMG_01_UC: track 0.00 -> 43.8 mm, vias 0 -> 2
- net /BATT_SENSE: track 0.00 -> 42.2 mm, vias 0 -> 2
- net MOTOR_02_EN: track 0.00 -> 40.8 mm, vias 0 -> 2
- net MOTOR_02_DIR: track 0.00 -> 40.6 mm, vias 0 -> 2
- net MOTOR_02_PWM: track 0.00 -> 40.4 mm, vias 0 -> 2
- net MOTOR_01_FAULT: track 0.00 -> 37.5 mm, vias 0 -> 1
- net EMG_02_UC: track 0.00 -> 35.5 mm, vias 0 -> 2
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- added copper zone on F.Cu, net +3V3
- added copper zone on F.Cu, net +5V
- added copper zone on F.Cu, net +BATT
- added copper zone on F.Cu, net BAT_P
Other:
- board text added: "+ -"
- board text added: "+ 1 -"
- board text added: "+ 2 -"
- board text added: "+ 3 -"
- board text added: "- s +"
- board text added: "-5V"
- board text added: "1"
- board text added: "2"
- board text added: "3"
- board text added: "3V3"
- board text added: "5V"
- board text added: "7.5V-16.8V"
- board text added: "BATT"
- board text added: "BTN"
- board text added: "CLK"
- board text added: "DIO"
- board text added: "EMG 1"
- board text added: "EMG 2"
- board text added: "GND"
- board text added: "HALL"
- board text added: "HAPTIC"
- board text added: "MOTORS"
- board text added: "OpenHand"
- board text added: "RST"
- board text added: "RX"
- board text added: "SCL"
- board text added: "SDA"
- board text added: "STM32F103RET6"
- board text added: "SWD"
- board text added: "TX"
- board text added: "USB C"
- board text added: "v2.0"
